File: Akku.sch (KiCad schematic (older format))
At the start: 25 parts

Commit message: Akku/PC aktualisiert
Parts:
- added D?: LED, symbol LED
- added R?: R, symbol R
- added SW?: SWITCH_INV, symbol SWITCH_INV
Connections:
- wire segments 96 -> 67
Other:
- moved on the sheet: D?, R?, U?, U?A

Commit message: Akku aktualisiert
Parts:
- added P? (x3): CONN_02X10, symbol CONN_02X10
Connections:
- net labels added: a0, a1, a2, a3, a4, a5, a6, a7
- wire segments 67 -> 113

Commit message: Akku Schaltplan aktualisiert
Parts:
- added D1, D2, D3: LED, symbol LED
- added R1, R10, R11, R2, R3, R4, R5, R6, R7, R8: R, symbol R
- added SW1, SW2: SWITCH_INV, symbol SWITCH_INV
- added U1, U2: 7400, symbol 7400
- added unit 1 of U3
- added unit 2 of U3
- added unit 3 of U3
- added unit 4 of U3
- gave numbers to parts that had none: 30
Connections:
- wire segments 113 -> 150
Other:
- note added: "(Akku)"
- note added: "(PC)"
- moved on the sheet: D10, D11, D12, D4, D5, D6, D7, D8, D9, P1, P2, P3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

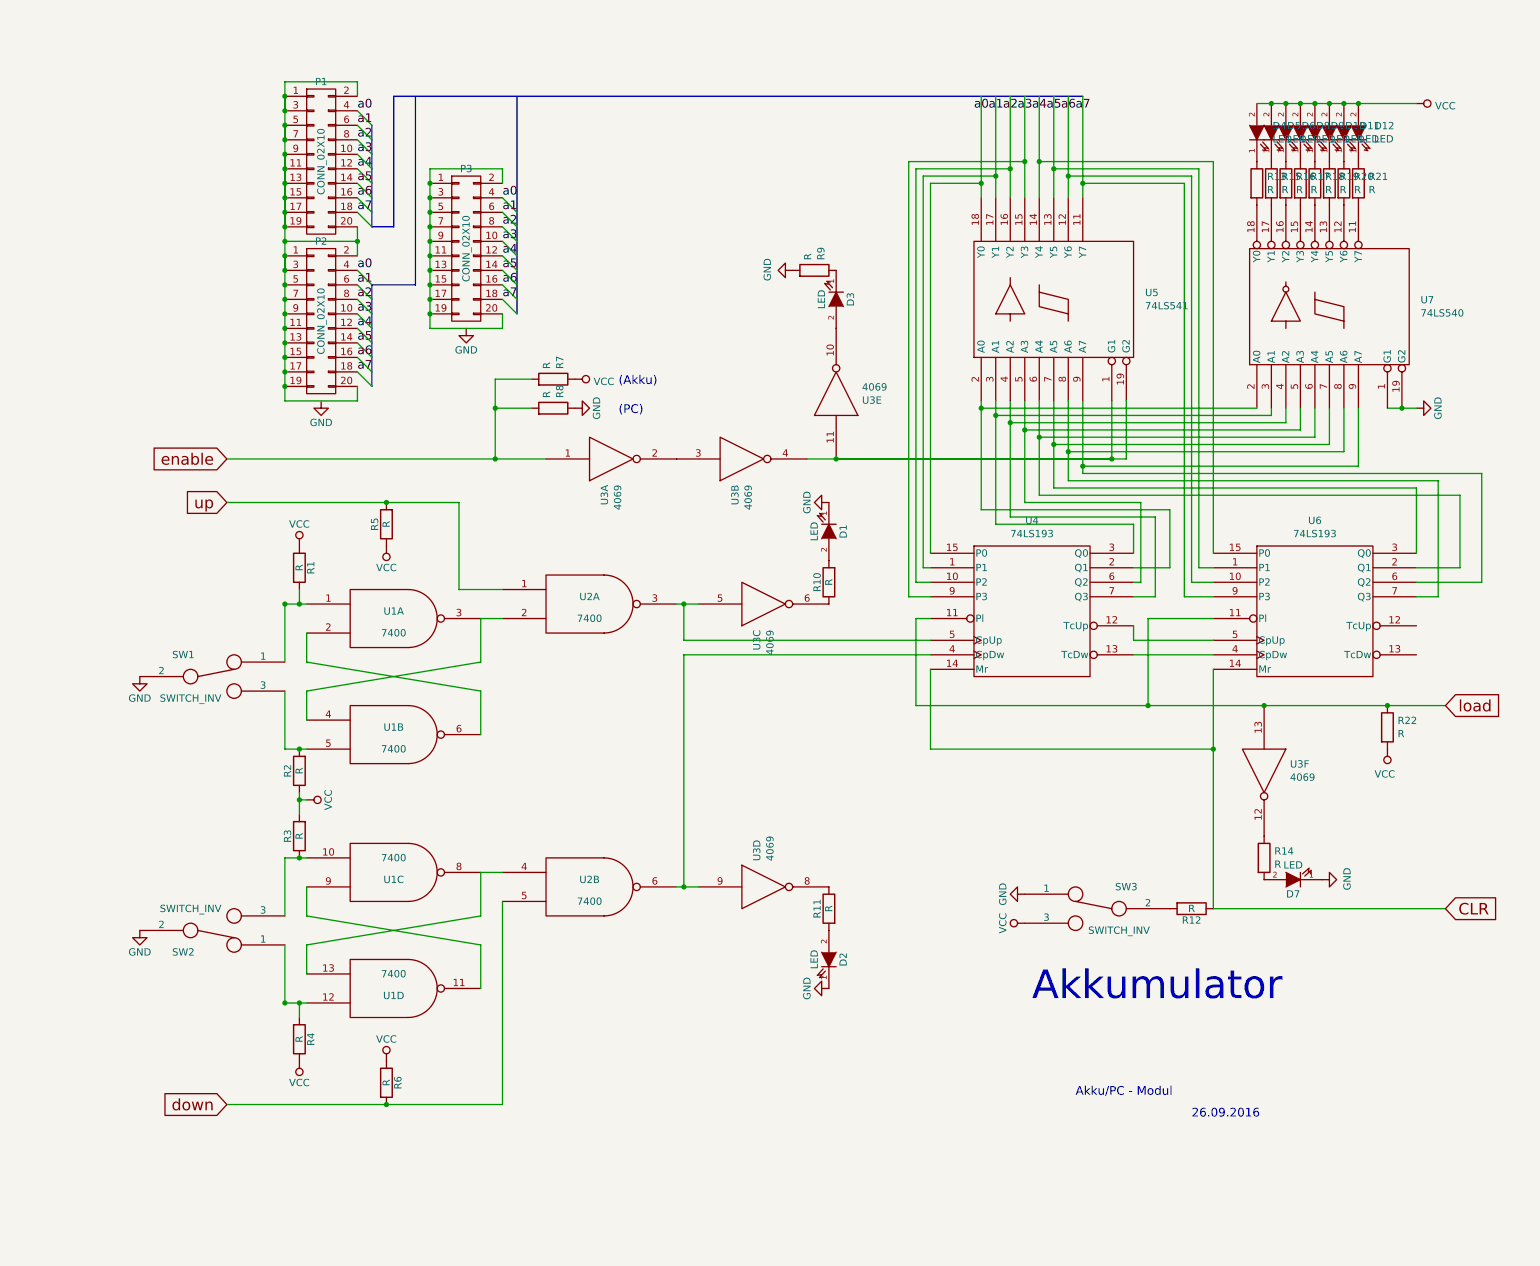
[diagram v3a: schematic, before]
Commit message: Schaltplan (wie mit T. Gatterer besprochen) fertiggestellt. Annotations. Footprints begonnen.
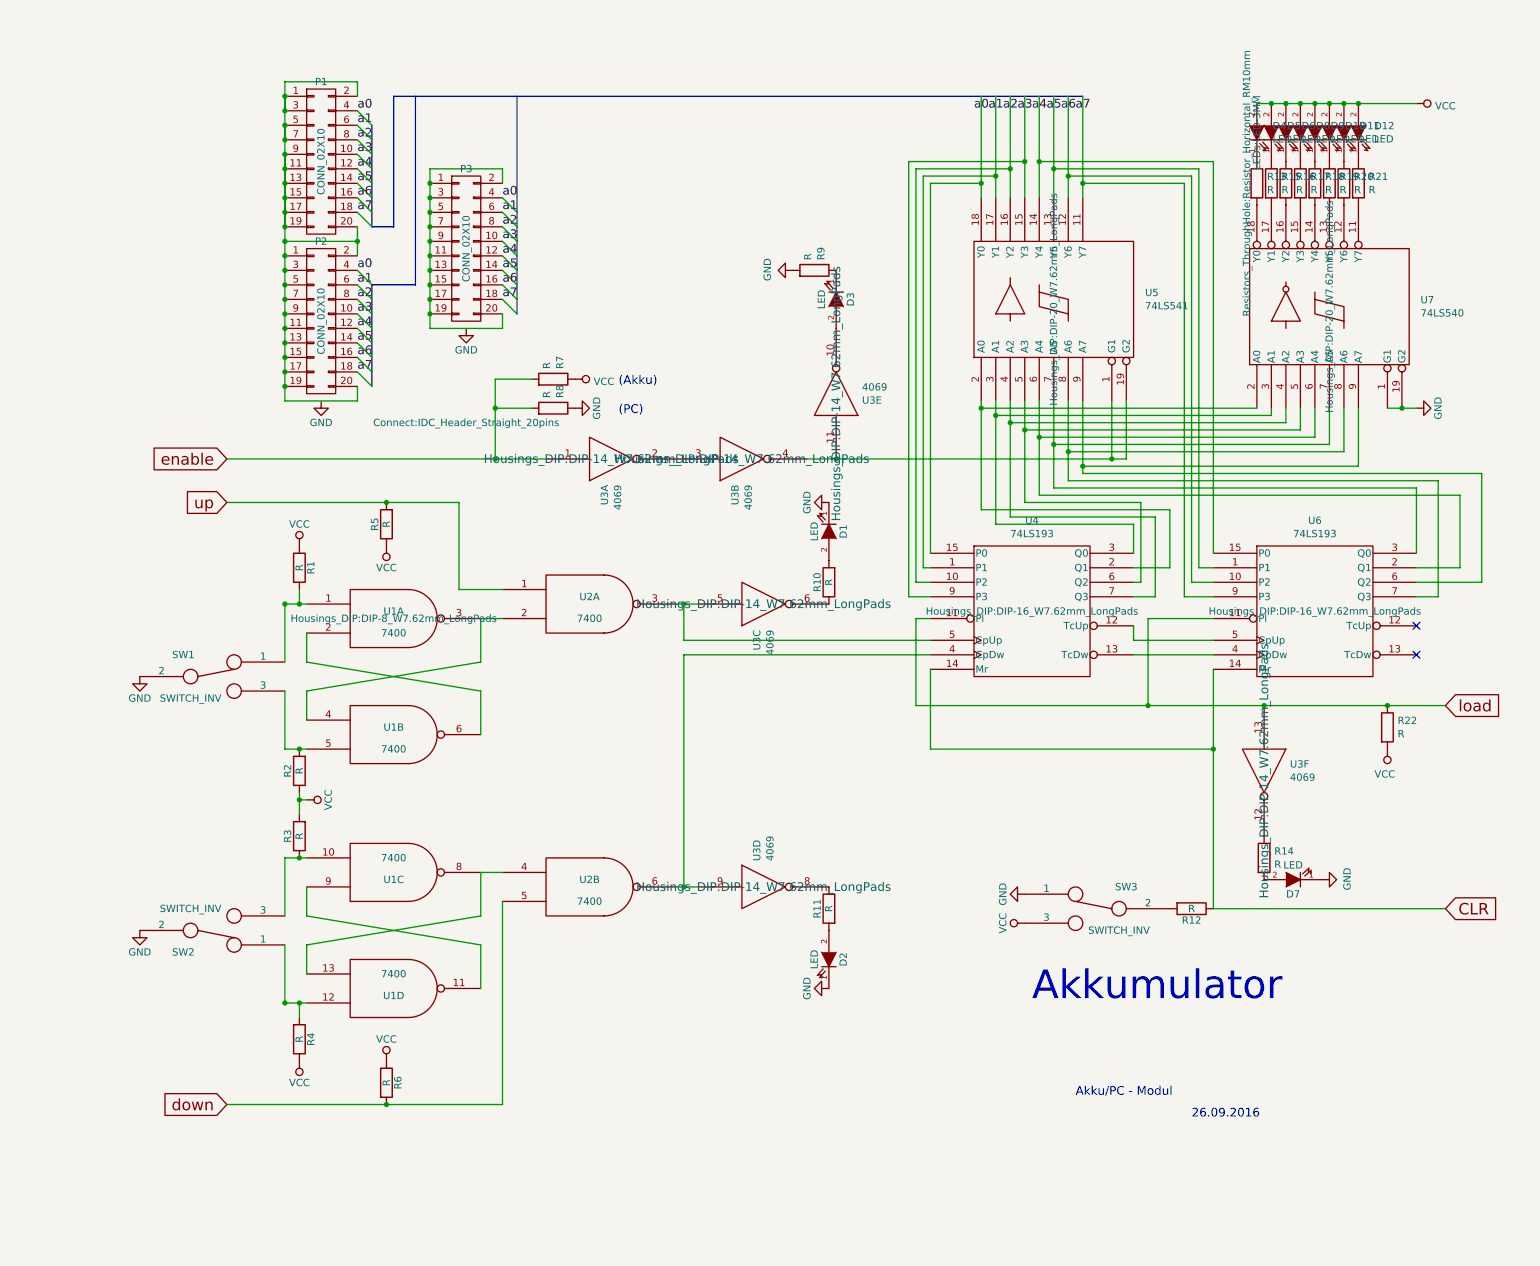
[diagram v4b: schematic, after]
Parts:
- D4: footprint (none) -> LEDs:LED-3MM
- P3: footprint (none) -> Connect:IDC_Header_Straight_20pins
- R13: footprint (none) -> Resistors_ThroughHole:Resistor_Horizontal_RM10mm
- U1: footprint (none) -> Housings_DIP:DIP-8_W7.62mm_LongPads
- U3: footprint (none) -> Housings_DIP:DIP-14_W7.62mm_LongPads
- U4, U6: footprint (none) -> Housings_DIP:DIP-16_W7.62mm_LongPads
- U5, U7: footprint (none) -> Housings_DIP:DIP-20_W7.62mm_LongPads
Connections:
- wire segments 150 -> 148
- no-connect marks 0 -> 2
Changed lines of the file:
@@
 F 0 "U7" V 9146 1422 50  0000 R CNN
 F 1 "74LS540" V 9055 1422 50  0000 R CNN
-F 2 "" H 9100 2050 50  0000 C CNN
+F 2 "Housings_DIP:DIP-20_W7.62mm_LongPads" H 9100 2050 50  0000 C CNN
 F 3 "" H 9100 2050 50  0000 C CNN
 	1    9100 2050
@@
 F 0 "D4" V 8646 742 50  0000 R CNN
 F 1 "LED" V 8555 742 50  0000 R CNN
-F 2 "" H 8600 850 50  0000 C CNN
+F 2 "LEDs:LED-3MM" H 8600 850 50  0000 C CNN
 F 3 "" H 8600 850 50  0000 C CNN
 	1    8600 850
@@
 F 0 "R13" H 8670 1246 50  0000 L CNN
 F 1 "R" H 8670 1155 50  0000 L CNN
-F 2 "" V 8530 1200 50  0000 C CNN
+F 2 "Resistors_ThroughHole:Resistor_Horizontal_RM10mm" V 8530 1200 50  0000 C CNN
 F 3 "" H 8600 1200 50  0000 C CNN
 	1    8600 1200
@@
 F 0 "U4" H 7050 4775 50  0000 C CNN
 F 1 "74LS193" H 7050 4684 50  0000 C CNN
-F 2 "" H 7050 4150 50  0000 C CNN
+F 2 "Housings_DIP:DIP-16_W7.62mm_LongPads" H 7050 4150 50  0000 C CNN
 F 3 "" H 7050 4150 50  0000 C CNN
 	1    7050 4150
@@
 F 0 "U6" H 9000 4775 50  0000 C CNN
 F 1 "74LS193" H 9000 4684 50  0000 C CNN
-F 2 "" H 9000 4150 50  0000 C CNN
+F 2 "Housings_DIP:DIP-16_W7.62mm_LongPads" H 9000 4150 50  0000 C CNN
 F 3 "" H 9000 4150 50  0000 C CNN
 	1    9000 4150
@@
 F 0 "U3" V 8604 5428 50  0000 L CNN
 F 1 "4069" V 8695 5428 50  0000 L CNN
-F 2 "" H 8650 5250 60  0001 C CNN
+F 2 "Housings_DIP:DIP-14_W7.62mm_LongPads" H 8650 5250 60  0000 C CNN
 F 3 "" H 8650 5250 60  0001 C CNN
 	6    8650 5250
@@
 F 0 "U3" V 5654 2828 50  0000 L CNN
 F 1 "4069" V 5745 2828 50  0000 L CNN
-F 2 "" H 5700 2650 60  0001 C CNN
+F 2 "Housings_DIP:DIP-14_W7.62mm_LongPads" H 5700 2650 60  0000 C CNN
 F 3 "" H 5700 2650 60  0001 C CNN
 	5    5700 2650
@@
 F 0 "U5" V 7246 1371 50  0000 R CNN
 F 1 "74LS541" V 7155 1371 50  0000 R CNN
-F 2 "" H 7200 2000 50  0000 C CNN
+F 2 "Housings_DIP:DIP-20_W7.62mm_LongPads" H 7200 2000 50  0000 C CNN
 F 3 "" H 7200 2000 50  0000 C CNN
 	1    7200 2000
@@
 F 0 "P3" H 3150 2200 50  0000 C CNN
 F 1 "CONN_02X10" V 3150 1650 50  0000 C CNN
-F 2 "" H 3150 450 50  0000 C CNN
+F 2 "Connect:IDC_Header_Straight_20pins" H 3150 450 50  0000 C CNN
 F 3 "" H 3150 450 50  0000 C CNN
 	1    3150 1650
@@
 F 0 "U3" V 4104 3278 50  0000 L CNN
 F 1 "4069" V 4195 3278 50  0000 L CNN
-F 2 "" H 4150 3100 60  0001 C CNN
+F 2 "Housings_DIP:DIP-14_W7.62mm_LongPads" H 4150 3100 60  0000 C CNN
 F 3 "" H 4150 3100 60  0001 C CNN
 	1    4150 3100
@@
 F 0 "U3" V 5004 3278 50  0000 L CNN
 F 1 "4069" V 5095 3278 50  0000 L CNN
-F 2 "" H 5050 3100 60  0001 C CNN
+F 2 "Housings_DIP:DIP-14_W7.62mm_LongPads" H 5050 3100 60  0000 C CNN
 F 3 "" H 5050 3100 60  0001 C CNN
 	2    5050 3100
@@
 F 0 "U1" H 2650 4250 50  0000 C CNN
 F 1 "7400" H 2650 4100 50  0000 C CNN
-F 2 "" H 2650 4200 50  0000 C CNN
+F 2 "Housings_DIP:DIP-8_W7.62mm_LongPads" H 2650 4200 50  0000 C CNN
 F 3 "" H 2650 4200 50  0000 C CNN
 	1    2650 4200
@@
 F 0 "U3" V 5154 4278 50  0000 L CNN
 F 1 "4069" V 5245 4278 50  0000 L CNN
-F 2 "" H 5200 4100 60  0001 C CNN
+F 2 "Housings_DIP:DIP-14_W7.62mm_LongPads" H 5200 4100 60  0000 C CNN
 F 3 "" H 5200 4100 60  0001 C CNN
 	3    5200 4100
@@
 F 0 "U3" V 5154 6228 50  0000 L CNN
 F 1 "4069" V 5245 6228 50  0000 L CNN
-F 2 "" H 5200 6050 60  0001 C CNN
+F 2 "Housings_DIP:DIP-14_W7.62mm_LongPads" H 5200 6050 60  0000 C CNN
 F 3 "" H 5200 6050 60  0001 C CNN
 	4    5200 6050
@@
 	8900 2900 7000 2900
 Wire Wire Line
-	7000 3400 7000 2700
-Wire Wire Line
-	7800 3400 7000 3400
-Wire Wire Line
-	7800 3950 7800 3400
+	7000 2700 7000 3400
+Wire Wire Line
+	7000 3400 7800 3400
+Wire Wire Line
+	7800 3400 7800 3950
 Wire Wire Line
 	7800 3950 7750 3950
@@
 	3400 7550 3400 6150
 Wire Wire Line
-	3100 3400 1500 3400
-Wire Wire Line
-	3100 4000 3100 3400
-Wire Wire Line
-	3400 4000 3100 4000
+	1500 3400 3100 3400
+Wire Wire Line
+	3100 3400 3100 4000
+Wire Wire Line
+	3100 4000 3400 4000
 Wire Wire Line
 	4650 4450 6350 4450
@@
 	1900 5850 2050 5850
 Wire Wire Line
-	2050 6850 1900 6850
+	1900 6850 2050 6850
 Wire Wire Line
 	2050 6450 3250 6250
@@
 	1900 5100 2050 5100
 Wire Wire Line
-	2050 4100 1900 4100
+	1900 4100 2050 4100
 Wire Wire Line
 	8300 6200 9900 6200
@@
 Connection ~ 5700 3100
 Wire Wire Line
-	7600 3100 5700 3100
+	5500 3100 7700 3100
 Wire Wire Line
 	1500 3100 3700 3100
@@
 	2900 1100 3400 1100
 Wire Wire Line
-	2900 2200 2900 1100
-Wire Wire Line
-	3400 2200 2900 2200
-Wire Wire Line
-	3400 2100 3400 2200
+	2900 1100 2900 2200
+Wire Wire Line
+	2900 2200 3400 2200
+Wire Wire Line
+	3400 2200 3400 2100
 Connection ~ 1900 2600
 Connection ~ 1900 2500
@@
 Connection ~ 1900 1800
 Wire Wire Line
-	1900 1700 1900 1800
+	1900 500  1900 2700
 Connection ~ 1900 700
 Connection ~ 1900 600
-Wire Wire Line
-	1900 700  1900 600
 Connection ~ 1900 900
 Connection ~ 1900 800
-Wire Wire Line
-	1900 900  1900 800
 Connection ~ 1900 1000
 Connection ~ 1900 1100
@@
 Connection ~ 1900 1500
 Connection ~ 1900 1400
+Connection ~ 1900 1600
+Wire Wire Line
+	2400 2700 2400 2600
+Wire Wire Line
+	1900 2700 2400 2700
+Wire Wire Line
+	2400 1500 2400 1700
+Wire Wire Line
+	1900 1600 2400 1600
+Wire Wire Line
+	1900 600  1900 700
+Wire Wire Line
+	1900 800  1900 900
 Wire Wire Line
 	1900 1000 1900 1500
-Connection ~ 1900 1600
-Wire Wire Line
-	2400 2700 2400 2600
-Wire Wire Line
-	1900 2700 2400 2700
-Wire Wire Line
-	2400 1500 2400 1700
-Wire Wire Line
-	1900 1600 2400 1600
-Wire Wire Line
-	1900 500  1900 2700
 Wire Wire Line
 	2400 500  1900 500
@@
 	7700 3100 7700 2700
 Wire Wire Line
-	5500 3100 7700 3100
-Wire Wire Line
 	7600 3100 7600 2700
 Connection ~ 7400 3150
@@
 Connection ~ 7200 3000
 Wire Wire Line
-	9700 3300 7200 3300
-Wire Wire Line
-	9700 3750 9700 3300
+	7200 3300 9700 3300
+Wire Wire Line
+	9700 3300 9700 3750
 Connection ~ 7100 2950
 Wire Wire Line
@@
 Connection ~ 6700 2750
 Wire Wire Line
-	8000 3450 6700 3450
-Wire Wire Line
-	8000 3850 8000 3450
+	6700 3450 8000 3450
+Wire Wire Line
+	8000 3450 8000 3850
 Wire Wire Line
 	7400 2700 7400 3200
@@
 	9300 2750 9300 3150
 Wire Wire Line
-	7200 3300 7200 2700
+	7200 2700 7200 3300
 Wire Wire Line
 	9100 3000 7200 3000
@@
 	6700 2750 8600 2750
 Wire Wire Line
-	6700 3450 6700 2700
+	6700 2700 6700 3450
 Connection ~ 8300 5100
 Wire Wire Line
@@
 Connection ~ 8700 650
 Wire Wire Line
-	7750 3850 8000 3850
+	8000 3850 7750 3850
 Wire Wire Line
 	10000 3350 10000 3850
@@
 Wire Wire Line
 	7750 4450 8300 4450
+NoConn ~ 9700 4250
+NoConn ~ 9700 4450
 $EndSCHEMATC
